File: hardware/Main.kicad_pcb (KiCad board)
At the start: 2 copper layers, 50 x 60 mm, 48 parts, among them Q1 DMG2305UX, SW1 Bourns PEC11R, SW2 Bourns PEC11R, U1 LM386, U3 RPi_Pico_TH, U4 S-1206B50-M3T1U, U5 RDA5807M_Module

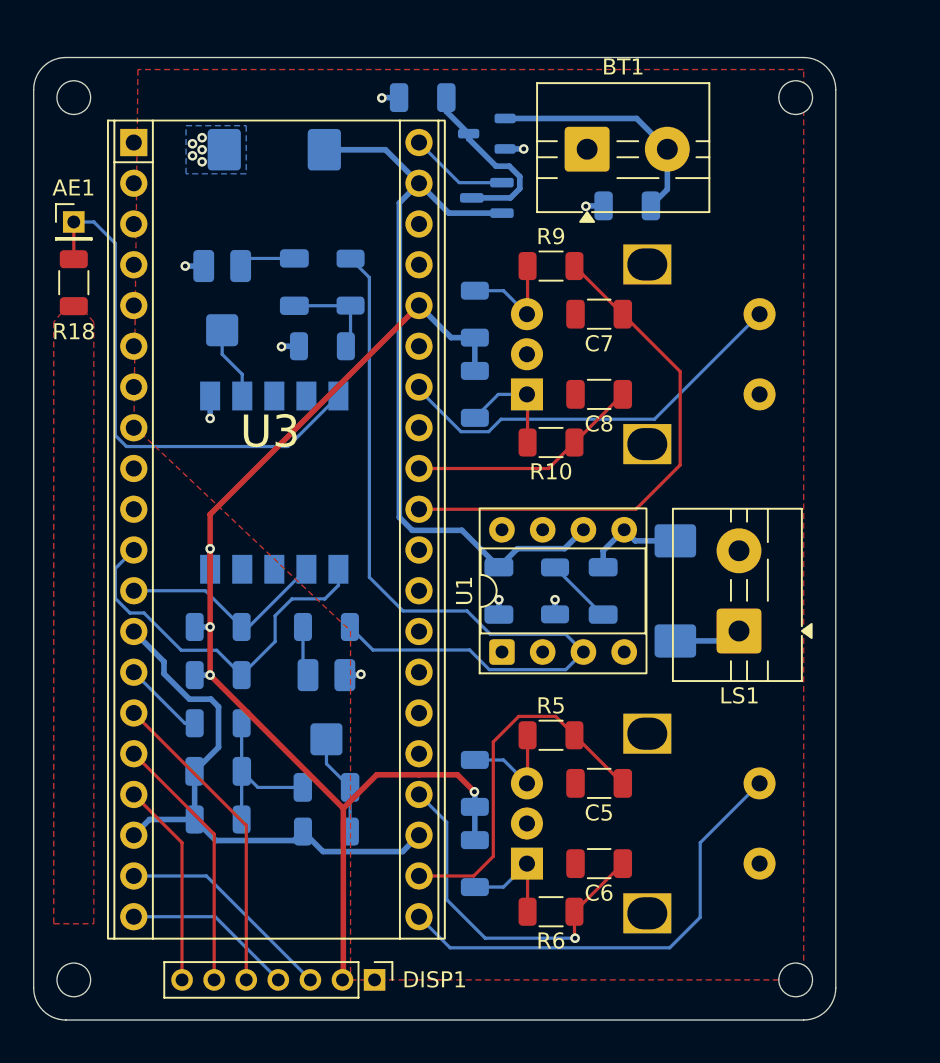
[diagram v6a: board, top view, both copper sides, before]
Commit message: pcb tweaks after TA tips
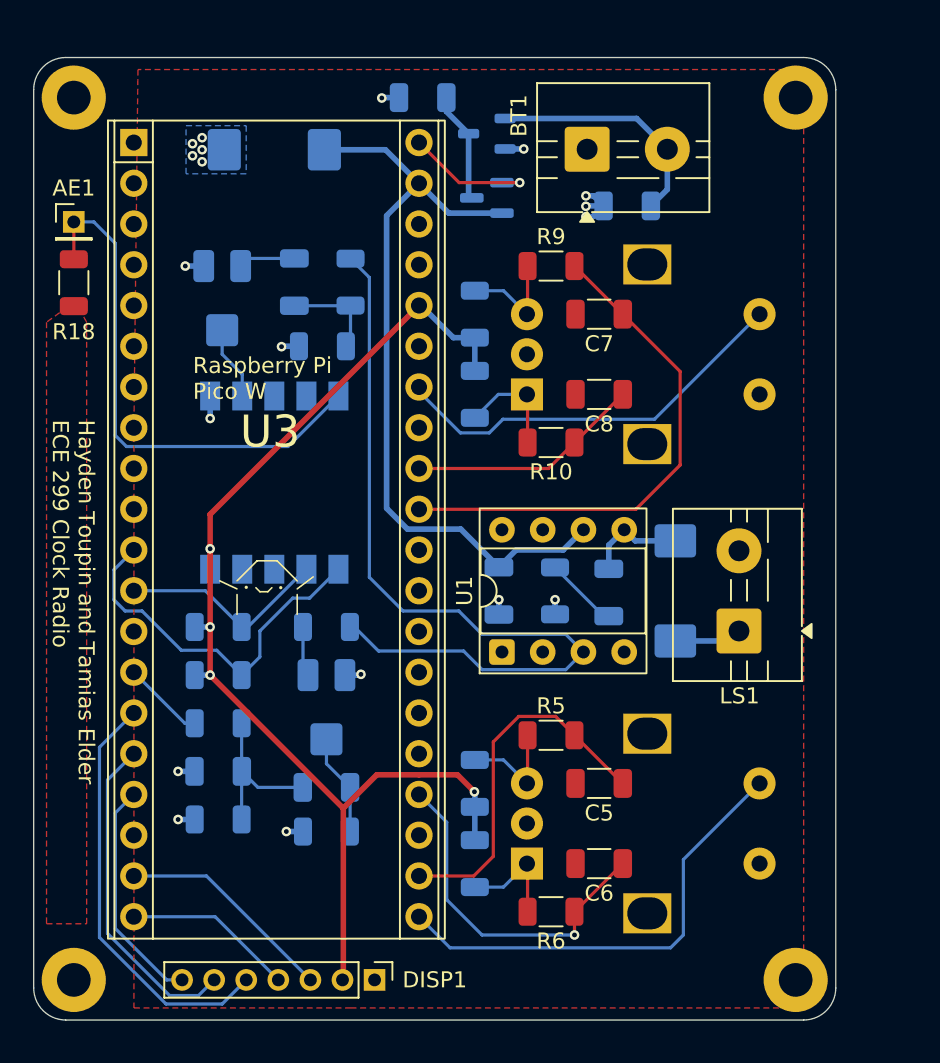
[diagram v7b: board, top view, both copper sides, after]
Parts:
- moved C2 0.36 mm to (153.3, 100.3)
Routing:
- net GND: track 45.1 -> 15.7 mm, vias 14 -> 19
- net /DISP_RES: track 19.5 -> 26.4 mm
- net Net-(Q1-D): track 11.3 -> 6.91 mm
- net /DISP_DC: track 16.2 -> 20.5 mm
- net /Power/VBUS: track 6.20 -> 8.43 mm, vias 0 -> 1
- net /DISP_CS: track 12.8 -> 14.3 mm
- net +5V: track 47.8 -> 48.6 mm
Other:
- board text added: "3v3"
- board text added: "CS"
- board text added: "DC"
- board text added: "GND"
- board text added: "Hayden Toupin and Tamias Elder ECE 299 Clock Radio"
- board text added: "PWM Audio"
- board text added: "RES"
- board text added: "Radio Audio"
- board text added: "Raspberry Pi Pico W"
- board text added: "SCL"
- board text added: "SDA"

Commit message: Minor Changes
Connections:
- U3 pad 22: /ENC1B -> /ENC1A
- U3 pad 24: /ENC1A -> /ENC1B
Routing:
- net /ENC1B: track 22.7 -> 16.5 mm
- net /ENC1A: track 21.9 -> 15.9 mm, vias 1 -> 0
- net +3.3V: track 73.0 -> 72.5 mm
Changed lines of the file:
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@@
 			)
 		)
-		(clearance 1)
+		(clearance 0.8)
 		(attr board_only exclude_from_pos_files exclude_from_bom allow_soldermask_bridges)
 		(fp_circle
@@
 			(layers "*.Cu" "*.Mask")
 			(remove_unused_layers no)
-			(net 10 "/ENC1B")
+			(net 11 "/ENC1A")
 			(pinfunction "GP17")
 			(pintype "bidirectional")
@@
 			(layers "*.Cu" "*.Mask")
 			(remove_unused_layers no)
-			(net 11 "/ENC1A")
+			(net 10 "/ENC1B")
 			(pinfunction "GP18")
 			(pintype "bidirectional")
@@
 	)
 	(segment
-		(start 146.15 109.66384)
-		(end 147.73984 108.074)
-		(width 0.2)
-		(layer "F.Cu")
-		(net 10)
-	)
-	(segment
 		(start 154.2125 112.25)
 		(end 154.225 112.25)
@@
 	)
 	(segment
-		(start 144.93 118.02)
-		(end 146.15 116.8)
+		(start 146.386 108.074)
+		(end 141.52 112.94)
 		(width 0.2)
 		(layer "F.Cu")
@@
 	)
 	(segment
-		(start 141.52 118.02)
-		(end 144.93 118.02)
+		(start 151.2125 109.25)
+		(end 150.0365 108.074)
 		(width 0.2)
 		(layer "F.Cu")
@@
 	(segment
 		(start 150.0365 108.074)
-		(end 151.2125 109.25)
+		(end 146.386 108.074)
 		(width 0.2)
 		(layer "F.Cu")
@@
 	)
 	(segment
-		(start 147.73984 108.074)
-		(end 150.0365 108.074)
+		(start 151.2125 120.25)
+		(end 149.9625 121.5)
 		(width 0.2)
 		(layer "F.Cu")
-		(net 10)
-	)
-	(segment
-		(start 146.15 116.8)
-		(end 146.15 109.66384)
-		(width 0.2)
-		(layer "F.Cu")
-		(net 10)
+		(net 11)
 	)
 	(segment
-		(start 151.2125 121.7)
-		(end 151.2125 120.25)
+		(start 145 121.5)
+		(end 141.52 118.02)
 		(width 0.2)
 		(layer "F.Cu")
@@
 	)
 	(segment
-		(start 151.225 120.25)
-		(end 151.2125 120.25)
+		(start 149.9625 121.5)
+		(end 145 121.5)
 		(width 0.2)
 		(layer "F.Cu")
 		(net 11)
 	)
-	(via
-		(at 151.2125 121.7)
-		(size 0.6)
-		(drill 0.3)
-		(layers "F.Cu" "B.Cu")
-		(net 11)
-	)
-	(segment
-		(start 151.2125 121.7)
-		(end 151.2125 121.7375)
-		(width 0.2)
-		(layer "B.Cu")
-		(net 11)
-	)
-	(segment
-		(start 145.45 121.7)
-		(end 143.25 119.5)
-		(width 0.2)
-		(layer "B.Cu")
-		(net 11)
-	)
-	(segment
-		(start 151.2125 121.7375)
-		(end 151.175 121.7)
-		(width 0.2)
-		(layer "B.Cu")
-		(net 11)
-	)
-	(segment
-		(start 151.175 121.7)
-		(end 145.45 121.7)
-		(width 0.2)
-		(layer "B.Cu")
-		(net 11)
-	)
 	(segment
-		(start 143.25 119.5)
-		(end 143.25 114.67)
-		(width 0.2)
-		(layer "B.Cu")
-		(net 11)
-	)
-	(segment
-		(start 143.25 114.67)
-		(end 141.52 112.94)
+		(start 151.225 120.25)
+		(end 151.2125 120.25)
 		(width 0.2)
-		(layer "B.Cu")
+		(layer "F.Cu")
 		(net 11)
 	)
@@
 	)
 	(segment
-		(start 143.914 111.714)
-		(end 144.975 112.775)
+		(start 144.975 112.775)
+		(end 143.55 114.2)
 		(width 0.35)
 		(layer "F.Cu")
@@
 	)
 	(segment
-		(start 138.886 111.714)
-		(end 141.525 111.714)
+		(start 137.2 114.2)
+		(end 136.8 113.8)
 		(width 0.35)
 		(layer "F.Cu")
@@
 	)
 	(segment
-		(start 141.525 111.714)
-		(end 143.914 111.714)
+		(start 143.55 114.2)
+		(end 137.2 114.2)
 		(width 0.35)
 		(layer "F.Cu")
@@
 		(width 0.35)
 		(layer "F.Cu")
-		(net 18)
-	)
-	(segment
-		(start 136.8 113.8)
-		(end 138.886 111.714)
-		(width 0.35)
-		(layer "F.Cu")
